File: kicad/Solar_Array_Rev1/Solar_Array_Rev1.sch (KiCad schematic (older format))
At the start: 30 parts, among them IC1 SPV1040, P1 CONN_01X02, P2 CONN_01X07, Q1 Q_NPN_BCE, U1 LTC2990

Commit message: Created Libs, Finished PCB Layout. -Created Solar_Array lib. -Finished layout for rev 1.0
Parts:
- removed D1, D4, D5, D6, D7, D8, D9: TVS, symbol TVS
- added IC2, IC3: NUP4202W1_4INPUT_TVS, TO_SOT_Packages_SMD:SC-70-6, symbol NUP4202W1_4INPUT_TVS
- C1, C2, C3, C4, C5, C6, C7: footprint (none) -> Capacitors_SMD:C_0603
- D2, D3: footprint (none) -> Diodes_SMD:SOD-323
- IC1: footprint TSSOP8 -> Solar:TSSOP-8; symbol SPV1040 -> SPV1040-RESCUE-Solar_Array_Rev1
- L1: footprint (none) -> Inductors:Inductor_1212
- P1: value CONN_01X02 -> PV_IN; footprint (none) -> Pin_Headers:Pin_Header_Straight_1x02
- P2: footprint (none) -> Pin_Headers:Pin_Header_Straight_1x07
- Q1: footprint (none) -> TO_SOT_Packages_SMD:SOT-23
- R1, R2, R3, R4, R5, R6, R7, R8: footprint (none) -> Resistors_SMD:R_0603
- U1: footprint (none) -> Solar:MSOP-16
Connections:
- wire segments 94 -> 115
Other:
- note added: "0-3.5V"
- note added: "1%"
- note added: "5V"
- note added: "ADR1"
- note added: "NC"
- note added: "SCL"
- note added: "SDA"
- note added: "VCC"
- note added: "Vout"
- note added: "XSHUT"
- moved on the sheet: P2

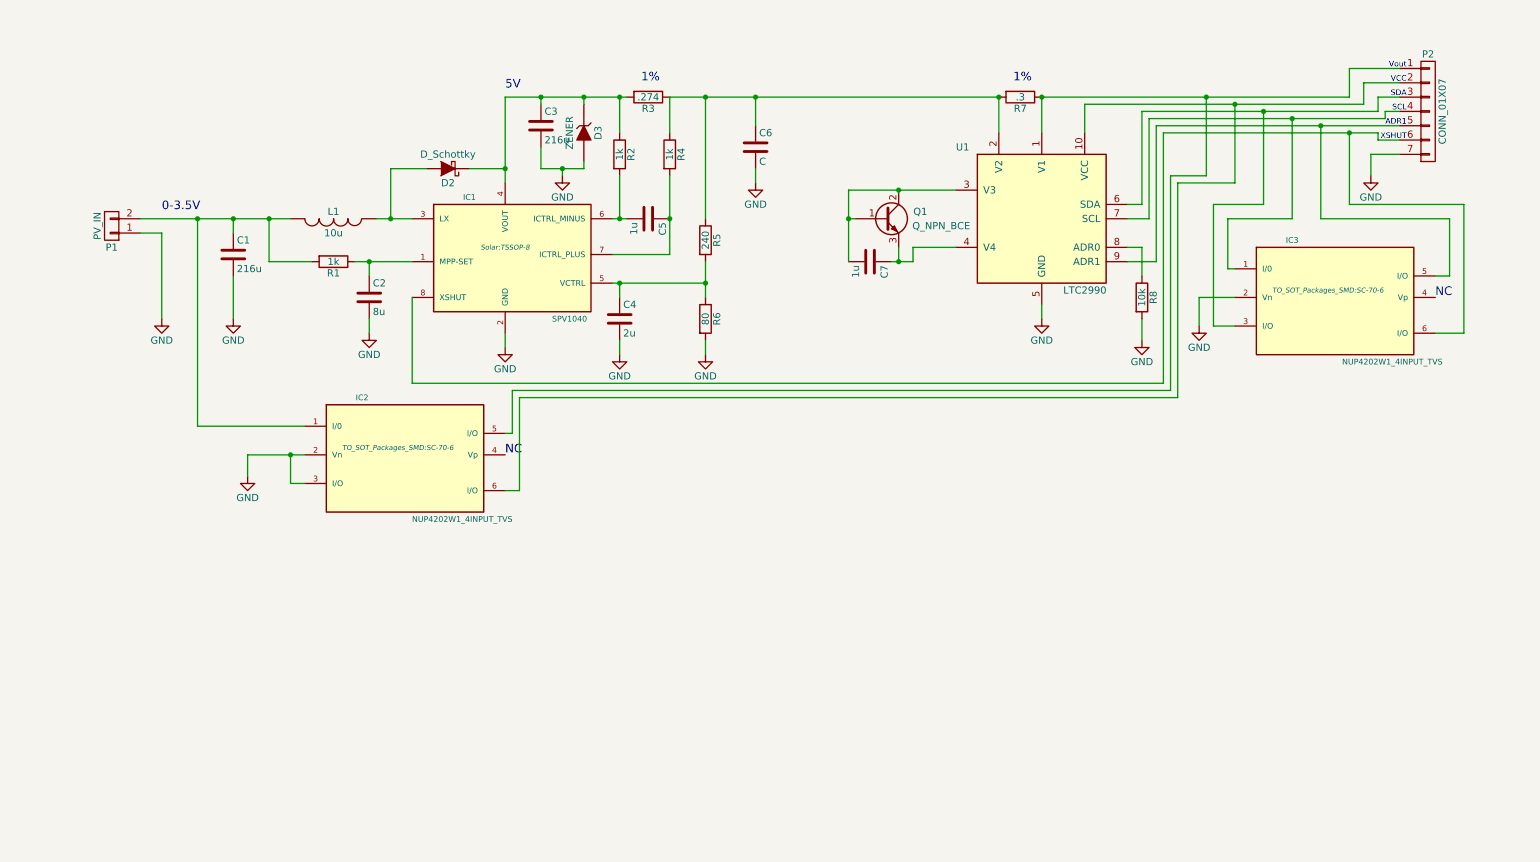
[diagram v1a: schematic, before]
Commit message: Added Rev1_BOM, added todo's to schematics
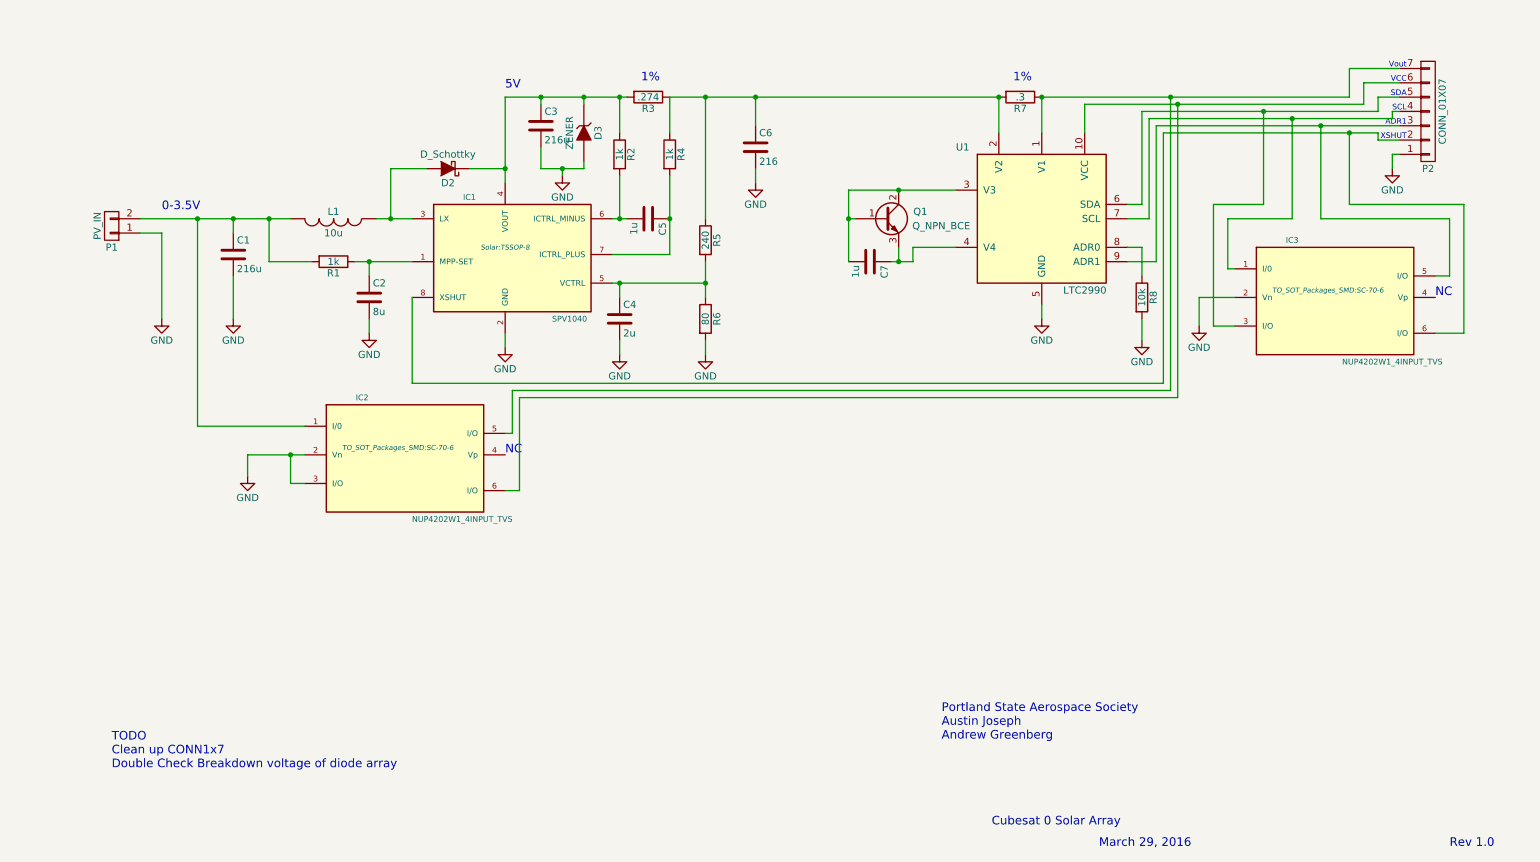
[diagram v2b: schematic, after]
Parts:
- C6: value C -> 216
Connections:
- net GND: now also P2.1 (P1); no longer P2.7 (P7)
- net at IC2.5 (I/O), R7.1, U1.1 (V1): now also P2.7 (P7); no longer P2.1 (P1)
- net at IC2.6 (I/O), U1.10 (VCC): now also P2.6 (P6); no longer P2.2 (P2)
- net at IC3.3 (I/O), U1.6 (SDA): now also P2.5 (P5); no longer P2.3 (P3)
- net at IC3.5 (I/O), U1.9 (ADR1): now also P2.3 (P3); no longer P2.5 (P5)
- net at IC1.8 (XSHUT), IC3.6 (I/O): now also P2.2 (P2); no longer P2.6 (P6)
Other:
- note added: "Cubesat 0 Solar Array"
- note added: "March 29, 2016"
- note added: "Portland State Aerospace Society\nAustin Joseph\nAndrew Greenberg"
- note added: "Rev 1.0"
- note added: "TODO\nClean up CONN1x7\nDouble Check Breakdown voltage of diode array"
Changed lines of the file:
@@
 P 5750 2750
 F 0 "C6" H 5775 2850 50  0000 L CNN
-F 1 "C" H 5775 2650 50  0000 L CNN
+F 1 "216" H 5775 2650 50  0000 L CNN
 F 2 "Capacitors_SMD:C_0603" H 5788 2600 50  0001 C CNN
 F 3 "" H 5750 2750 50  0000 C CNN
@@
 	8500 3250 8500 2550
 Wire Wire Line
-	8500 2550 10150 2550
+	8500 2550 10200 2550
 $Comp
 L GND #PWR08
@@
 F 3 "" H 10450 2500 50  0000 C CNN
 	1    10450 2500
-	1    0    0    -1
+	1    0    0    1
 $EndComp
 Wire Wire Line
@@
 	8450 2500 10100 2500
 Wire Wire Line
-	10100 2500 10100 2400
-Wire Wire Line
 	10100 2400 10250 2400
 Wire Wire Line
-	10150 2550 10150 2500
-Wire Wire Line
 	3350 3800 3350 4400
 Wire Wire Line
@@
 Wire Wire Line
 	10100 2700 10250 2700
-Wire Wire Line
-	10050 2800 10250 2800
-Wire Wire Line
-	10050 2800 10050 2950
 $Comp
 L GND #PWR010
 U 1 1 56FCEB98
-P 10050 2950
-F 0 "#PWR010" H 10050 2700 50  0001 C CNN
-F 1 "GND" H 10050 2800 50  0000 C CNN
-F 2 "" H 10050 2950 50  0000 C CNN
-F 3 "" H 10050 2950 50  0000 C CNN
-	1    10050 2950
-	1    0    0    -1
-$EndComp
-Wire Wire Line
-	8900 2950 8900 2400
-Connection ~ 8900 2400
-Wire Wire Line
-	9100 2450 9100 3000
-Connection ~ 9100 2450
+P 10200 2900
+F 0 "#PWR010" H 10200 2650 50  0001 C CNN
+F 1 "GND" H 10200 2750 50  0000 C CNN
+F 2 "" H 10200 2900 50  0000 C CNN
+F 3 "" H 10200 2900 50  0000 C CNN
+	1    10200 2900
+	1    0    0    -1
+$EndComp
 Wire Wire Line
 	9300 2500 9300 3150
@@
 	4050 4450 8650 4450
 Wire Wire Line
-	8650 4450 8650 2950
-Wire Wire Line
-	8650 2950 8900 2950
+	8650 4450 8650 2400
 Wire Wire Line
 	4000 5150 4100 5150
@@
 Wire Wire Line
 	4100 4500 8700 4500
-Wire Wire Line
-	8700 4500 8700 3000
-Wire Wire Line
-	8700 3000 9100 3000
 $Comp
 L GND #PWR012
@@
 Text Notes 1600 3200 0    60   ~ 0
 0-3.5V
-Wire Wire Line
-	10150 2500 10250 2500
 Text Notes 10300 2200 2    39   ~ 0
 Vout
@@
 Text Notes 10300 2400 2    39   ~ 0
 SDA
-Text Notes 10300 2500 2    39   ~ 0
-SCL
 Text Notes 10300 2600 2    39   ~ 0
 ADR1
 Text Notes 10300 2700 2    39   ~ 0
 XSHUT
+Text Notes 7400 7500 0    60   ~ 0
+Cubesat 0 Solar Array
+Text Notes 10600 7650 0    60   ~ 0
+Rev 1.0
+Text Notes 8150 7650 0    60   ~ 0
+March 29, 2016
+Text Notes 7050 6900 0    60   ~ 0
+Portland State Aerospace Society\nAustin Joseph\nAndrew Greenberg
+Wire Wire Line
+	10100 2500 10100 2400
+Text Notes 10300 2500 2    39   ~ 0
+SCL
+Wire Wire Line
+	10200 2550 10200 2500
+Wire Wire Line
+	10200 2500 10250 2500
+Wire Wire Line
+	10200 2800 10200 2900
+Wire Wire Line
+	10250 2800 10200 2800
+Connection ~ 8650 2400
+Wire Wire Line
+	8700 4500 8700 2450
+Connection ~ 8700 2450
+Text Notes 1250 7100 0    60   ~ 0
+TODO\nClean up CONN1x7\nDouble Check Breakdown voltage of diode array
 $EndSCHEMATC

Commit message: Updated Component values to reflect design doc.
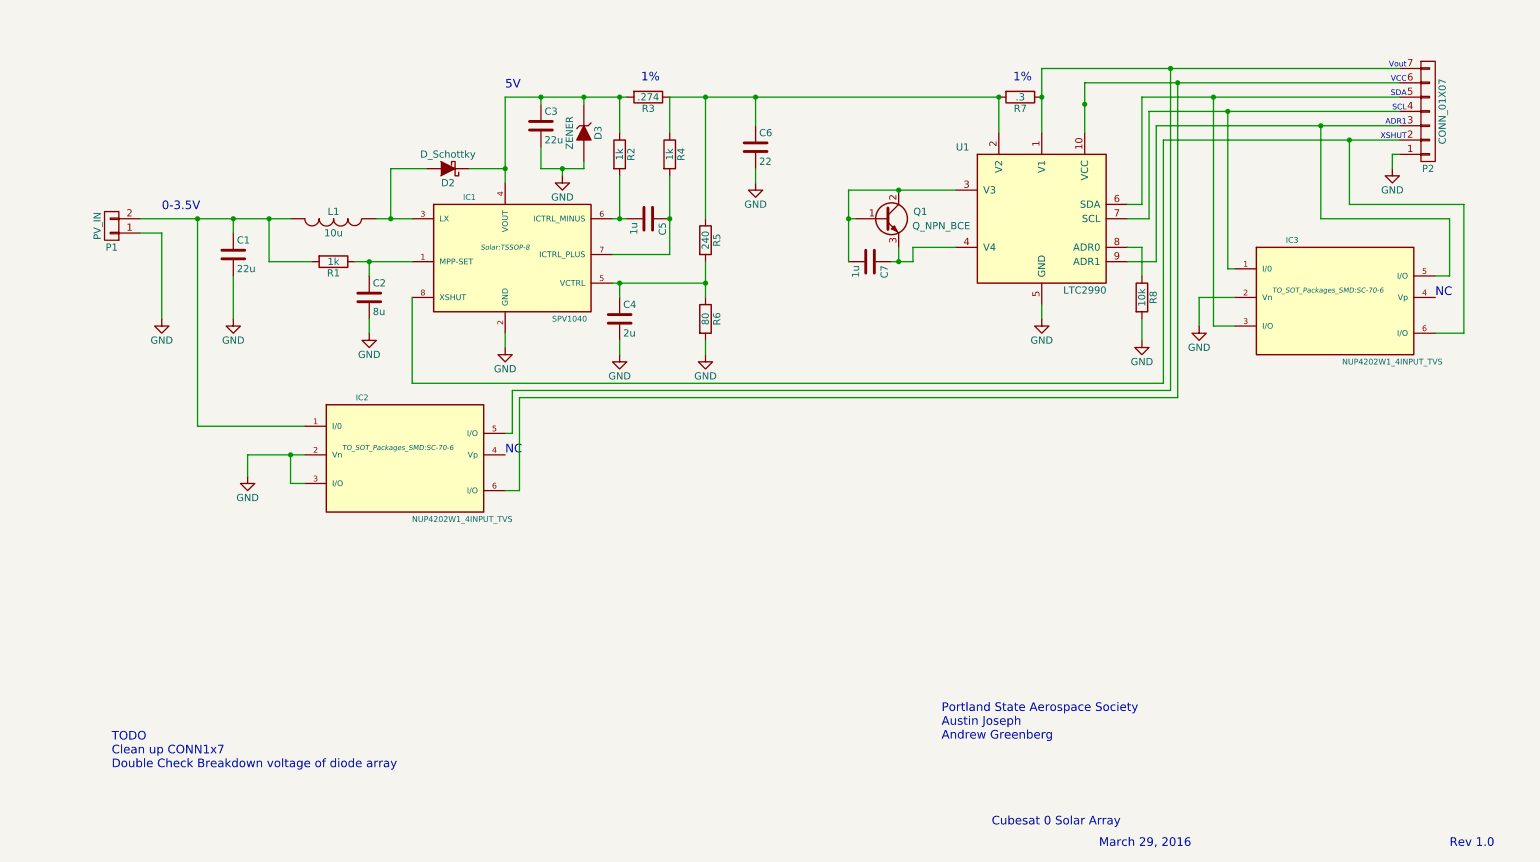
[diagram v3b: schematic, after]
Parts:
- C1, C3: value 216u -> 22u
- C6: value 216 -> 22
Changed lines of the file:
@@
 P 2100 3500
 F 0 "C1" H 2125 3600 50  0000 L CNN
-F 1 "216u" H 2125 3400 50  0000 L CNN
+F 1 "22u" H 2125 3400 50  0000 L CNN
 F 2 "Capacitors_SMD:C_0603" H 2138 3350 50  0001 C CNN
 F 3 "" H 2100 3500 50  0000 C CNN
@@
 P 4250 2600
 F 0 "C3" H 4275 2700 50  0000 L CNN
-F 1 "216u" H 4275 2500 50  0000 L CNN
+F 1 "22u" H 4275 2500 50  0000 L CNN
 F 2 "Capacitors_SMD:C_0603" H 4288 2450 50  0001 C CNN
 F 3 "" H 4250 2600 50  0000 C CNN
@@
 P 5750 2750
 F 0 "C6" H 5775 2850 50  0000 L CNN
-F 1 "216" H 5775 2650 50  0000 L CNN
+F 1 "22" H 5775 2650 50  0000 L CNN
 F 2 "Capacitors_SMD:C_0603" H 5788 2600 50  0001 C CNN
 F 3 "" H 5750 2750 50  0000 C CNN
@@
 Connection ~ 5750 2400
 Wire Wire Line
-	7750 2400 7750 2650
+	7750 2200 7750 2650
 Connection ~ 7450 2400
 Connection ~ 7750 2400
@@
 	5150 2400 7450 2400
 Wire Wire Line
-	7750 2400 9900 2400
-Wire Wire Line
-	8050 2650 8050 2450
-Wire Wire Line
-	8050 2450 10000 2450
-Wire Wire Line
-	8350 3150 8450 3150
-Wire Wire Line
-	8450 3150 8450 2500
-Wire Wire Line
-	8350 3250 8500 3250
-Wire Wire Line
-	8500 3250 8500 2550
-Wire Wire Line
-	8500 2550 10200 2550
+	8050 2300 8050 2650
+Wire Wire Line
+	8450 3150 8350 3150
+Wire Wire Line
+	8450 2400 8450 3150
+Wire Wire Line
+	8500 3250 8350 3250
+Wire Wire Line
+	8500 2500 8500 3250
 $Comp
 L GND #PWR08
@@
 $EndComp
 Wire Wire Line
-	9900 2400 9900 2200
-Wire Wire Line
-	9900 2200 10250 2200
-Wire Wire Line
-	10000 2450 10000 2300
-Wire Wire Line
-	10000 2300 10250 2300
-Wire Wire Line
-	8450 2500 10100 2500
-Wire Wire Line
-	10100 2400 10250 2400
+	7750 2200 10250 2200
+Wire Wire Line
+	8050 2300 10250 2300
+Wire Wire Line
+	8450 2400 10250 2400
 Wire Wire Line
 	3350 3800 3350 4400
@@
 	3350 4400 8600 4400
 Wire Wire Line
-	8600 4400 8600 2650
-Wire Wire Line
-	8600 2650 10100 2650
-Wire Wire Line
-	10100 2650 10100 2700
-Wire Wire Line
-	10100 2700 10250 2700
+	8600 2700 10250 2700
 $Comp
 L GND #PWR010
@@
 $EndComp
 Wire Wire Line
-	9300 2500 9300 3150
-Connection ~ 9300 2500
-Wire Wire Line
-	9500 2550 9500 3250
-Connection ~ 9500 2550
-Wire Wire Line
 	9700 2600 9700 3250
 Connection ~ 9700 2600
-Wire Wire Line
-	9900 2650 9900 3150
-Connection ~ 9900 2650
 $Comp
 L C C4
@@
 	10700 3150 9900 3150
 Wire Wire Line
-	9100 3600 9050 3600
-Wire Wire Line
-	9050 3600 9050 3250
-Wire Wire Line
-	9050 3250 9500 3250
-Wire Wire Line
-	9100 4000 8950 4000
-Wire Wire Line
-	8950 4000 8950 3150
-Wire Wire Line
-	8950 3150 9300 3150
+	9050 3600 9100 3600
+Wire Wire Line
+	9050 2500 9050 3600
+Wire Wire Line
+	8950 4000 9100 4000
+Wire Wire Line
+	8950 2400 8950 4000
 Wire Wire Line
 	1850 3250 1850 4700
@@
 	4050 4450 8650 4450
 Wire Wire Line
-	8650 4450 8650 2400
+	8650 4450 8650 2200
 Wire Wire Line
 	4000 5150 4100 5150
@@
 Text Notes 7050 6900 0    60   ~ 0
 Portland State Aerospace Society\nAustin Joseph\nAndrew Greenberg
-Wire Wire Line
-	10100 2500 10100 2400
 Text Notes 10300 2500 2    39   ~ 0
 SCL
 Wire Wire Line
-	10200 2550 10200 2500
-Wire Wire Line
-	10200 2500 10250 2500
+	8500 2500 10250 2500
 Wire Wire Line
 	10200 2800 10200 2900
 Wire Wire Line
 	10250 2800 10200 2800
-Connection ~ 8650 2400
-Wire Wire Line
-	8700 4500 8700 2450
-Connection ~ 8700 2450
+Wire Wire Line
+	8700 4500 8700 2300
 Text Notes 1250 7100 0    60   ~ 0
 TODO\nClean up CONN1x7\nDouble Check Breakdown voltage of diode array
+Connection ~ 8650 2200
+Connection ~ 8050 2450
+Connection ~ 8700 2300
+Wire Wire Line
+	8600 4400 8600 2700
+Connection ~ 8950 2400
+Connection ~ 9050 2500
+Wire Wire Line
+	9900 3150 9900 2700
+Connection ~ 9900 2700
 $EndSCHEMATC

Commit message: Updated component vals.  Added filter Caps, TVS array
-Updated and used //47uF for in/out filters.
-Added more robust shutdown. XShut tied to input.
-Introduced TVS array on schematics.
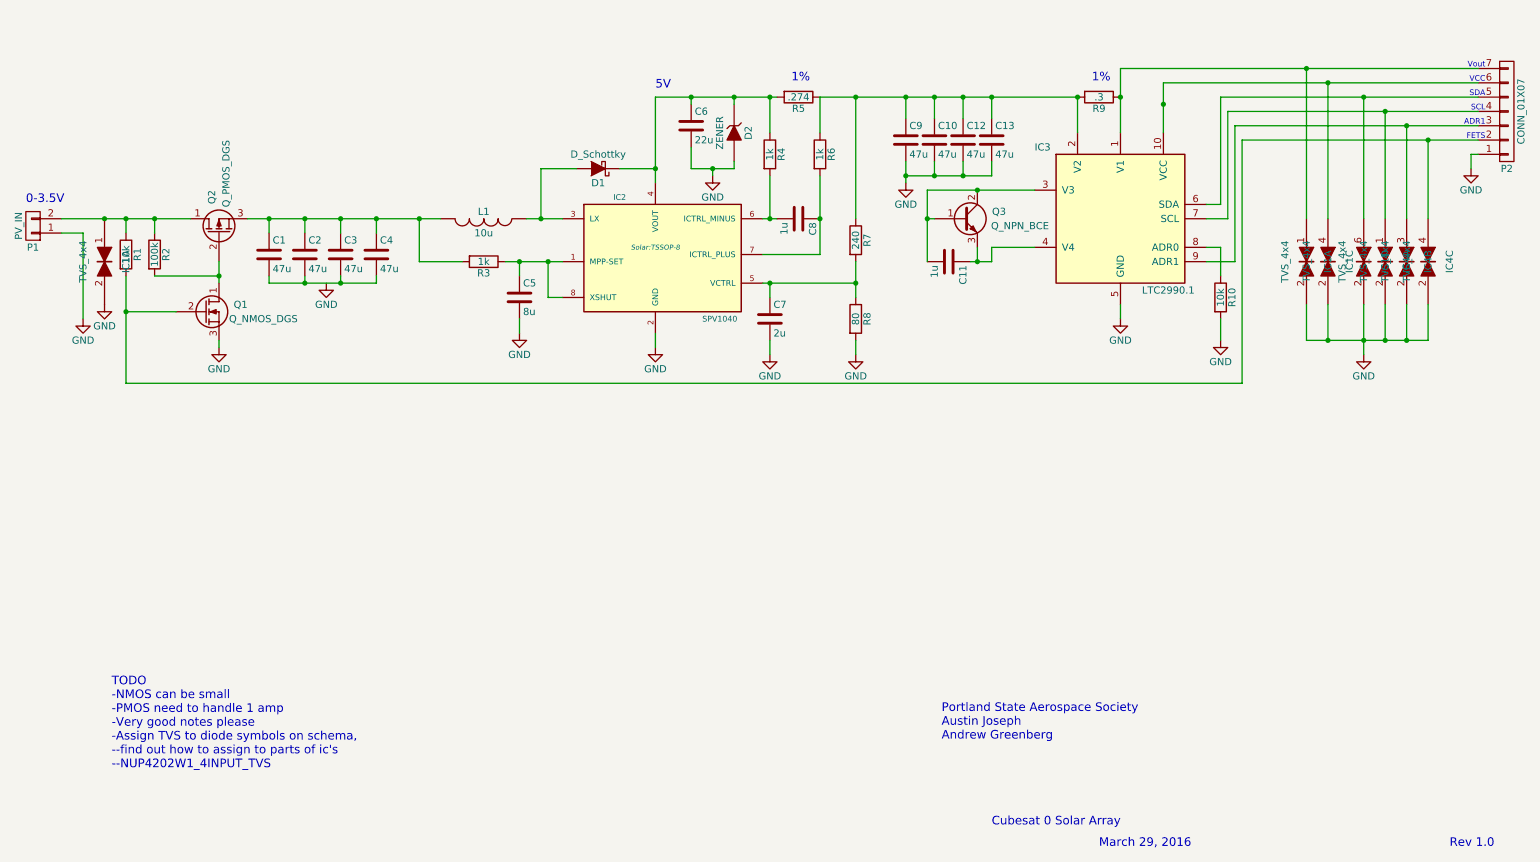
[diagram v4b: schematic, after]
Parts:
- removed IC2, IC3: NUP4202W1_4INPUT_TVS, TO_SOT_Packages_SMD:SC-70-6, symbol NUP4202W1_4INPUT_TVS
- removed U1: LTC2990, Solar:MSOP-16, symbol LTC2990
- added C10, C12, C13, C2, C3, C4: 47u, Capacitors_SMD:C_0805, symbol C
- added IC1 (x2), IC4: TVS_4x4, TO_SOT_Packages_SMD:SC-70-6, symbol TVS_4x4
- added IC3: LTC2990.1, Solar:MSOP-10, symbol LTC2990.1
- added Q1: Q_NMOS_DGS, symbol Q_NMOS_DGS
- added Q2: Q_PMOS_DGS, symbol Q_PMOS_DGS
- added R1: 10k, Resistors_SMD:R_0603, symbol R
- added R2: 100k, Resistors_SMD:R_0603, symbol R
- C1: value 22u -> 47u; footprint Capacitors_SMD:C_0603 -> Capacitors_SMD:C_0805
- C6: renamed from C3; footprint Capacitors_SMD:C_0603 -> Capacitors_SMD:C_0805
- C9: renamed from C6; value 22 -> 47u; footprint Capacitors_SMD:C_0603 -> Capacitors_SMD:C_0805
- renumbered C7 to C11, C2 to C5, C4 to C7, C5 to C8, D2 to D1, D3 to D2, IC1 to IC2, Q1 to Q3, R8 to R10, R1 to R3, R2 to R4, R3 to R5, R4 to R6, R5 to R7, R6 to R8, R7 to R9
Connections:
- net GND: now also C10.2, C12.2, C13.2, IC1.2, IC1.2, IC1.2, IC1.2, IC3.5 (GND), IC4.2, IC4.2, IC4.2, Q1.3 (S); no longer C1.2
- net at P2.7 (P7), R9.1: now also IC1.1, IC3.1 (V1)
- net at P2.6 (P6): now also IC1.4, IC3.10 (VCC)
- net at C9.1, R5.1, R6.1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: now also C10.1, C12.1, C13.1, IC3.2 (V2)
- net at C11.2, Q3.1 (B), Q3.2 (C): now also IC3.3 (V3)
- net at C11.1, Q3.3 (E): now also IC3.4 (V4)
- net at P2.5 (P5): now also IC1.6, IC3.6 (SDA)
- net at P2.4 (P4): now also IC3.7 (SCL), IC4.1
- net at R10.1: now also IC3.8 (ADR0)
- net at P2.3 (P3): now also IC3.9 (ADR1), IC4.3
- net at C5.1, IC2.1 (MPP-SET), R3.1: now also IC2.8 (XSHUT)
- net at P2.2 (P2): now also IC4.4, Q1.2 (G), R1.2; no longer IC2.8 (XSHUT)
- net at C1.1, L1.2, R3.2: now also C2.1, C3.1, C4.1, Q2.3 (S); no longer P1.2 (P2)
- new net: C1.2, C2.2, C3.2, C4.2
- new net: IC1.1, P1.2 (P2), Q2.1 (D), R1.1, R2.1
- new net: Q1.1 (D), Q2.2 (G), R2.2
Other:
- note added: "FETS"
- note added: "TODO\n-NMOS can be small\n-PMOS need to handle 1 amp\n-Very good notes please\n-Assign TVS to diode symbols on schema, \n--find out how to assign to parts of ic's\n--NUP4202W1_4INPUT_TVS\n"
- note removed: "NC"
- note removed: "TODO\nClean up CONN1x7\nDouble Check Breakdown voltage of diode array"
- note removed: "XSHUT"
- moved on the sheet: C1, C11, C5, C6, C7, C8, C9, D1, D2, IC2, L1, P1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
